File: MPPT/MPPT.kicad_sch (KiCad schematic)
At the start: 29 parts, among them U1 TPS7H4010MRNPTSEP, U2 5962L1620901VYC

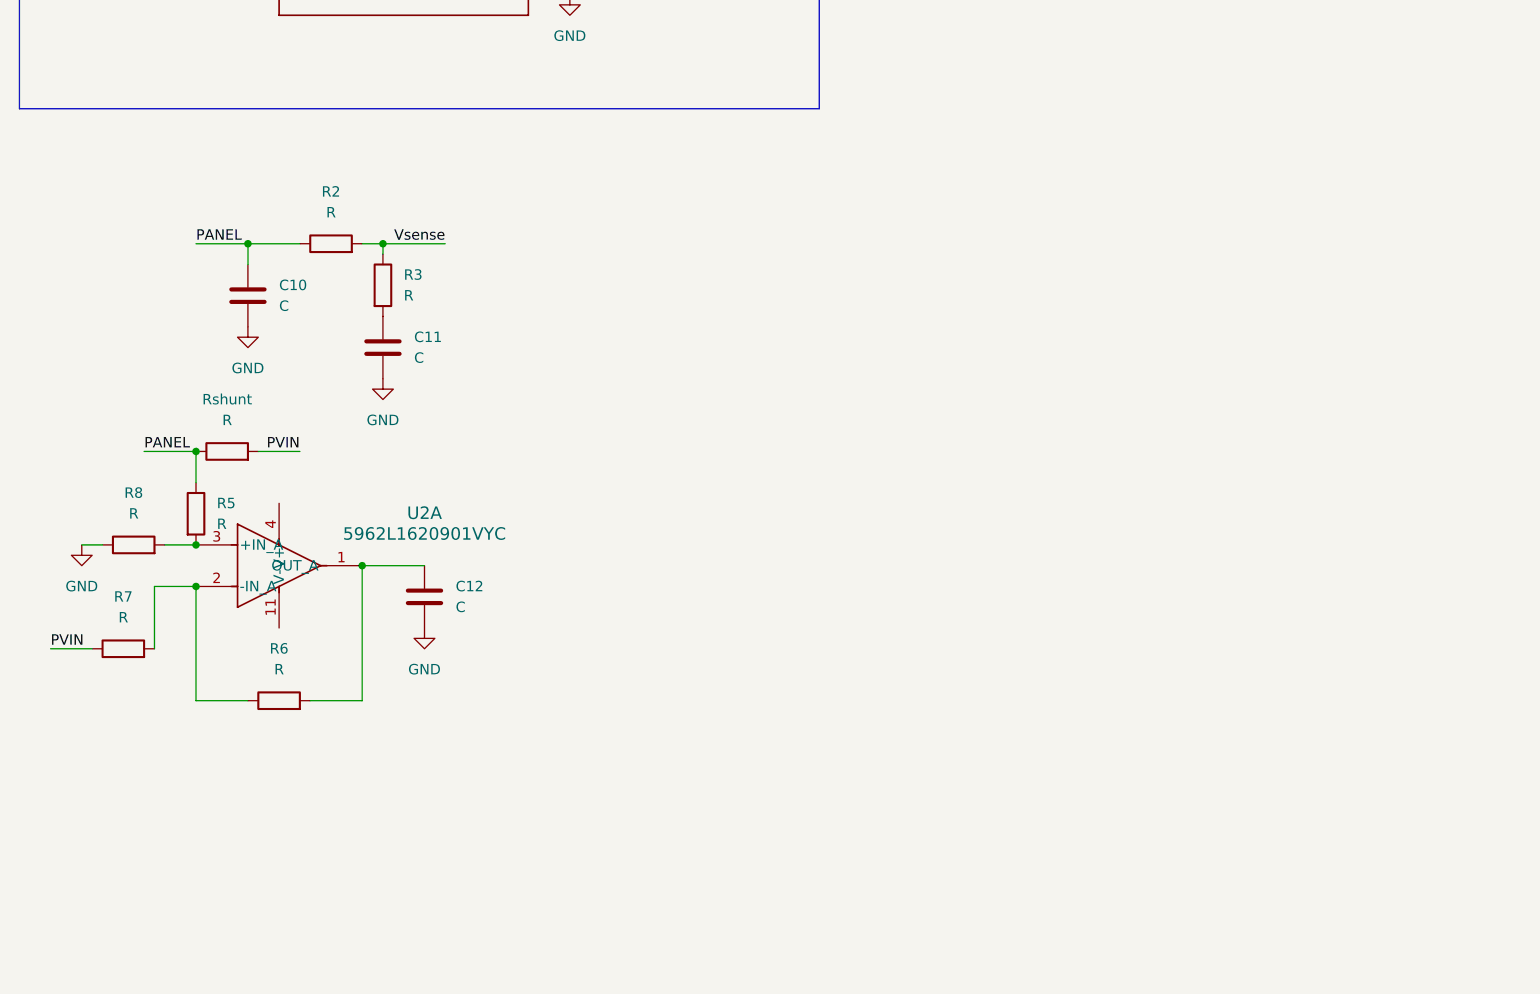
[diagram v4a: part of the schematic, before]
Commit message: Se añaden los amplificadores analógicos y un sumador
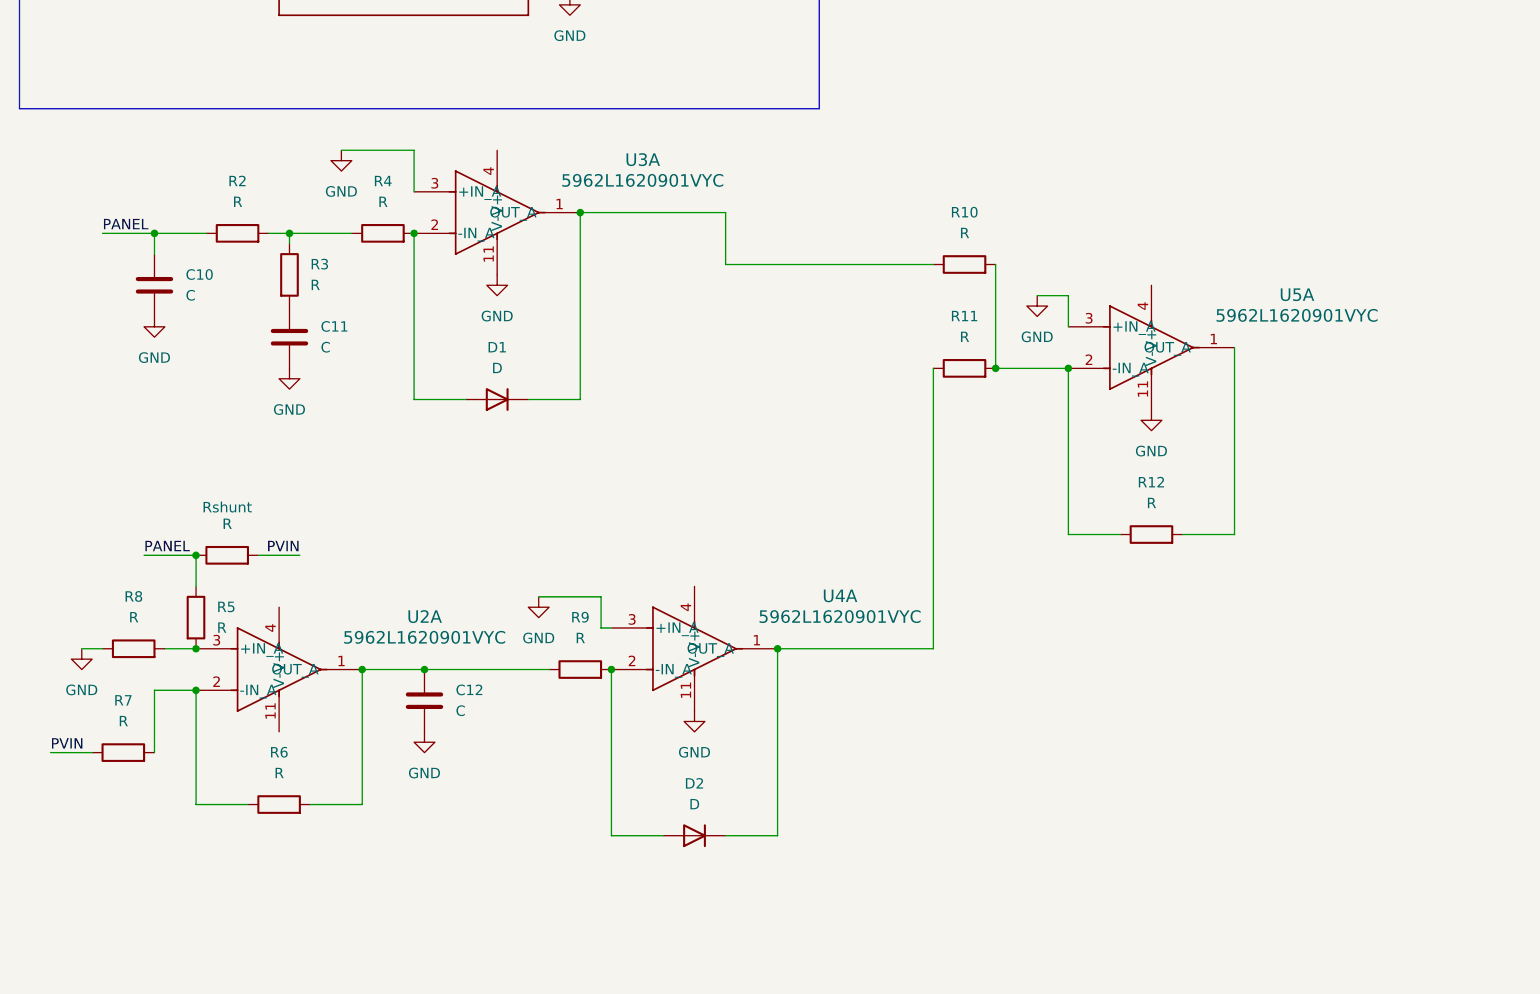
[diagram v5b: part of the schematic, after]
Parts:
- added D1, D2: D, symbol Device:D
- added R10, R11, R12, R4, R9: R, symbol Device:R
- added U3, U4, U5: 5962L1620901VYC, HFR0014A-IPC_A, symbol 5962L1620901VYC:5962L1620901VYC
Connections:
- net GND: now also U3.11 (V-), U3.3 (+IN_A), U4.11 (V-), U4.3 (+IN_A), U5.11 (V-), U5.3 (+IN_A)
- net at C12.1, R6.2, U2.1 (OUT_A): now also R9.1
- net Vsense: no longer names the net of R2.2, R3.1
- net Vsense: now also R4.1
- new net: D2.1 (K), R11.1, U4.1 (OUT_A)
- new net: D2.2 (A), R9.2, U4.2 (-IN_A)
- new net: R10.2, R11.2, R12.1, U5.2 (-IN_A)
- new net: D1.1 (K), R10.1, U3.1 (OUT_A)
- new net: D1.2 (A), R4.2, U3.2 (-IN_A)
- new net: R12.2, U5.1 (OUT_A)
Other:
- moved on the sheet: C10, C11, C12, R2, R3, R5, R6, R7, R8, Rshunt, U2A

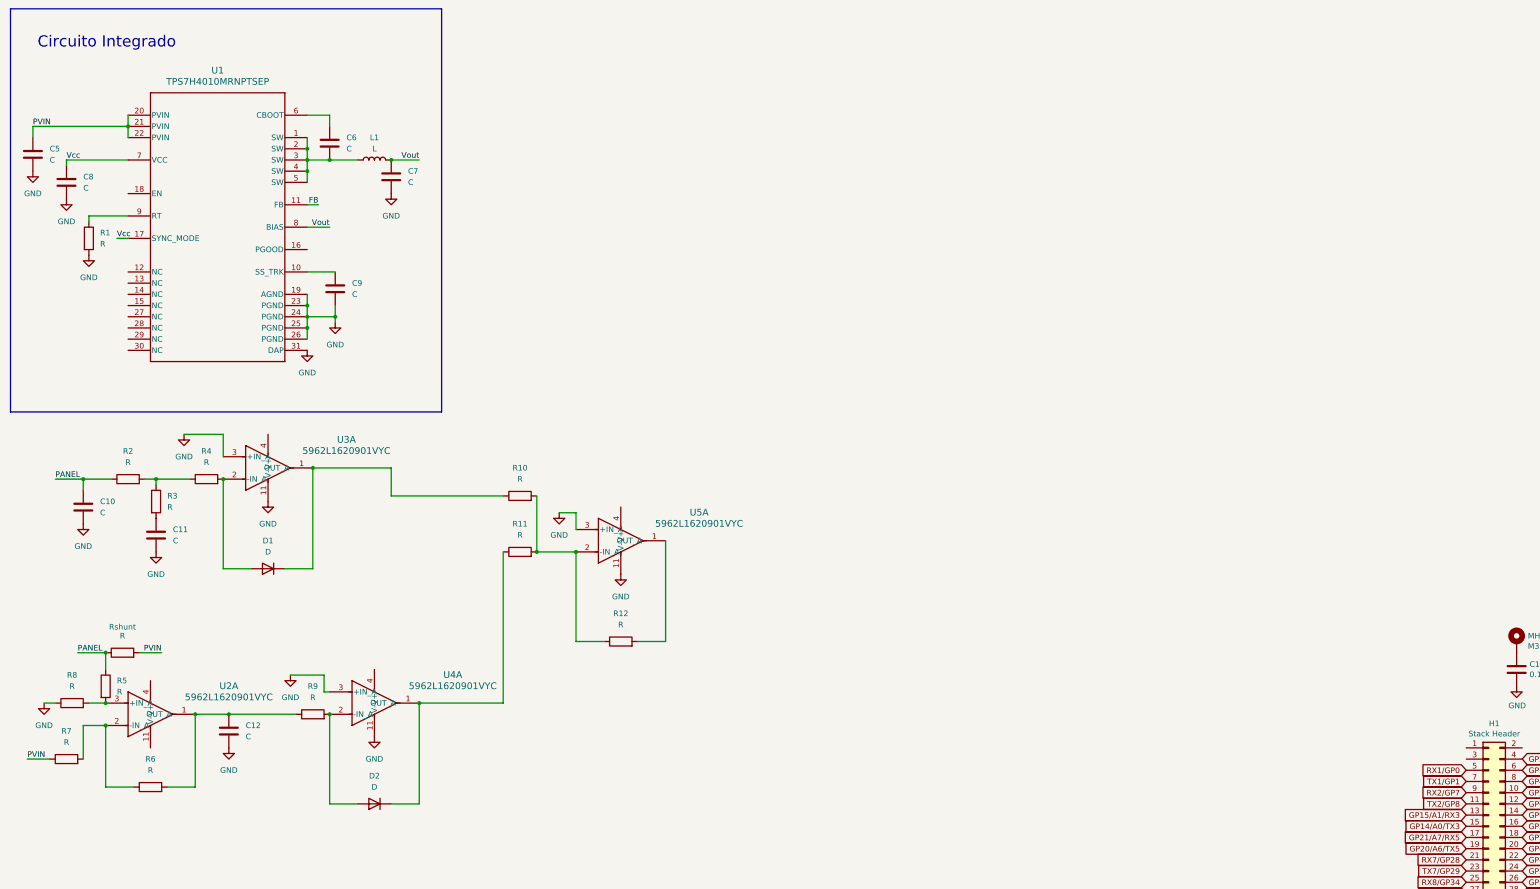
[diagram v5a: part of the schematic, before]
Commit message: Se termina el censado de potencia de entrada
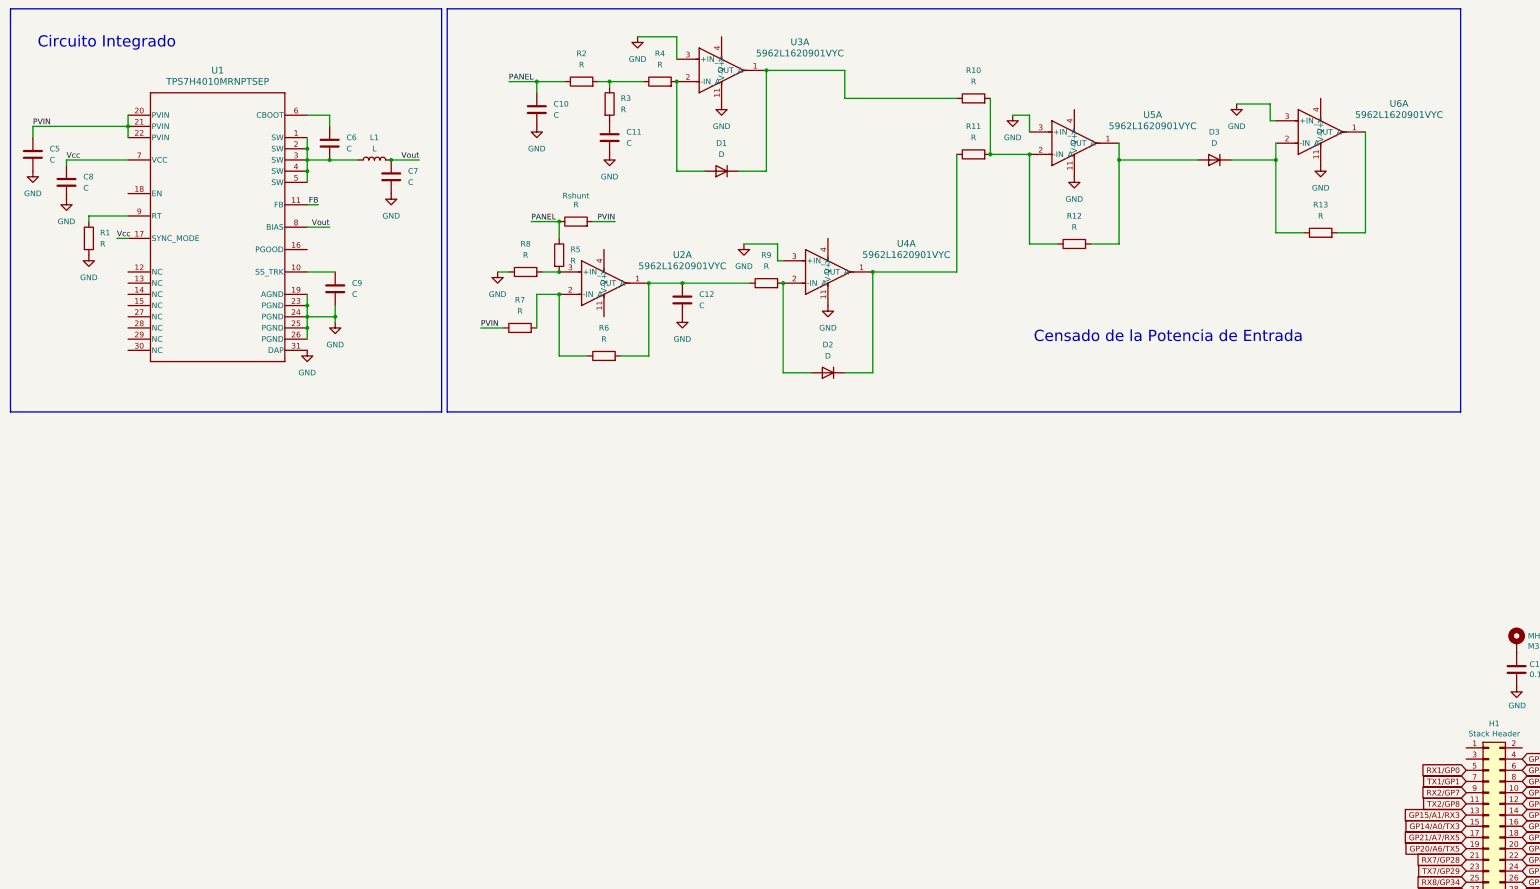
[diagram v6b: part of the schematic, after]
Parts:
- added D3: D, symbol Device:D
- added R13: R, symbol Device:R
- added U6: 5962L1620901VYC, HFR0014A-IPC_A, symbol 5962L1620901VYC:5962L1620901VYC
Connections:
- net GND: now also U6.11 (V-), U6.3 (+IN_A)
- net at R12.2, U5.1 (OUT_A): now also D3.2 (A)
- new net: R13.2, U6.1 (OUT_A)
- new net: D3.1 (K), R13.1, U6.2 (-IN_A)
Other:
- note added: "Censado de la Potencia de Entrada"
- moved on the sheet: C10, C11, C12, D1, D2, R10, R11, R12, R2, R3, R4, R5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

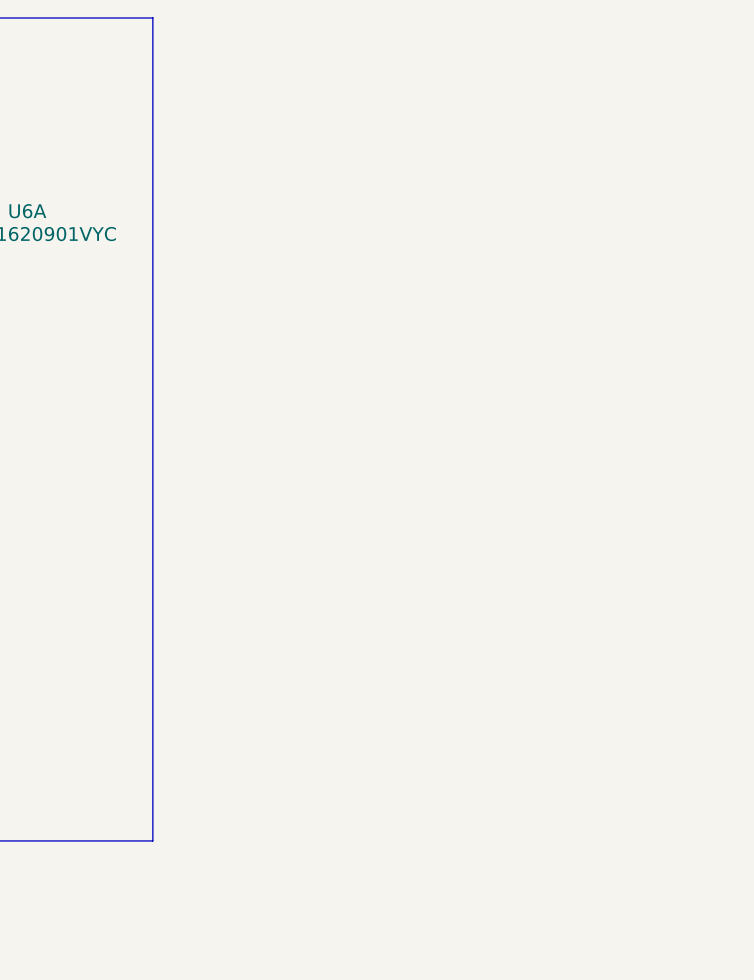
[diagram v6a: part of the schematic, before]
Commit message: Se crea un restador y un retardo
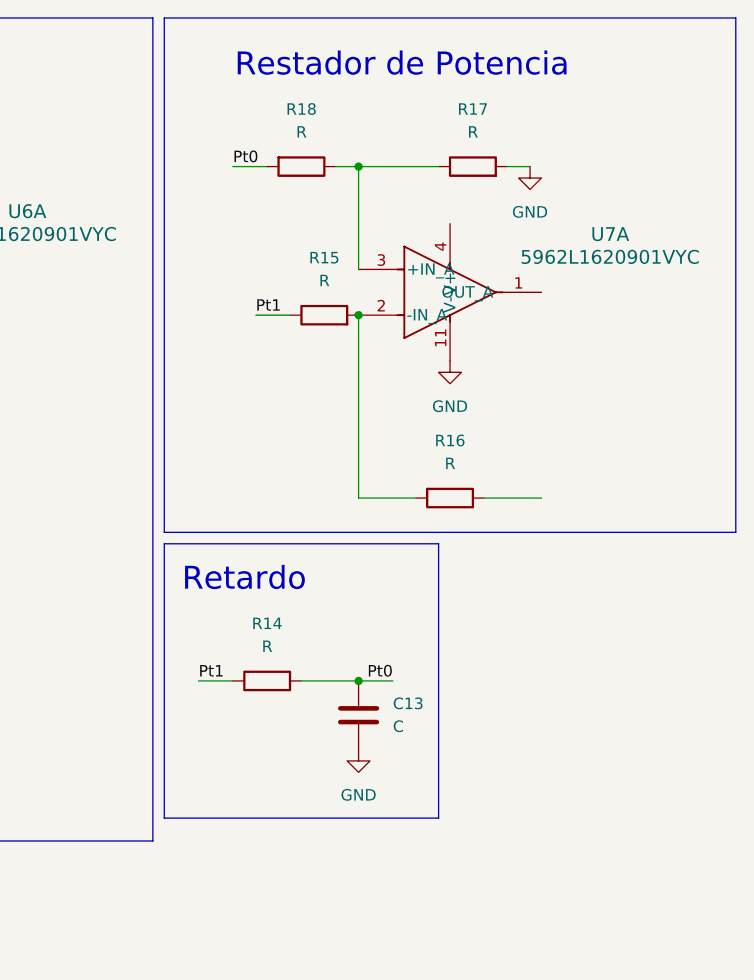
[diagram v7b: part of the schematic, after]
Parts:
- added C13: C, symbol Device:C
- added R14, R15, R16, R17, R18: R, symbol Device:R
- added U7: 5962L1620901VYC, HFR0014A-IPC_A, symbol 5962L1620901VYC:5962L1620901VYC
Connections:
- net GND: now also C13.2, R17.2, U7.11 (V-)
- new net: R15.2, R16.2, U7.2 (-IN_A)
- new net: R17.1, R18.1, U7.3 (+IN_A)
- new net Pt0: C13.1, R14.2, R18.2
- new net Pt1: R14.1, R15.1
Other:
- note added: "Restador de Potencia"
- note added: "Retardo"
